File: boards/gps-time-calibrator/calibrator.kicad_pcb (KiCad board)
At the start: 4 copper layers, 180 x 100 mm, 374 parts, among them J1 DF40C-40DP-0.4V(51), J2 DF40C(2.0)-40DS-0.4V(51), J3 USB-C 5V/3A + DATA, J5 GPS ANTENNA, J6 INPUT 5V / 2.5V THRESHOLD, J7 FPGA OUTPUT 5V, J8 61300411121, Q1 AO3400A, Q10 AO3400A, Q11 AO3400A, Q12 AO3400A, Q13 AO3400A, Q14 AO3400A, Q15 AO3400A, Q16 AO3400A, Q2 AO3400A, Q3 AO3400A, Q4 AO3400A, Q5 AO3400A, Q6 AO3400A, Q7 AO3400A, Q8 AO3400A, Q9 AO3400A, U1 USBLC6-2SC6, U10 SN74AHCT1G125DBVR, U11 HUSB238_002DD, U12 AP2112K-3.3, U14 TPS259531DSGR, U15 TPS7A4533DCQR, U2 AP2112K-3.3, U3 SN74LVC541APWR, U4 SN74LVC541APWR, U5 AP2112K-3.3, U6 MAX-M10S-00B-01, U7 SN74LVC1G17DBVR, U9 TLV3501AIDBVR, Y1 AOC97FAJC-10.0000

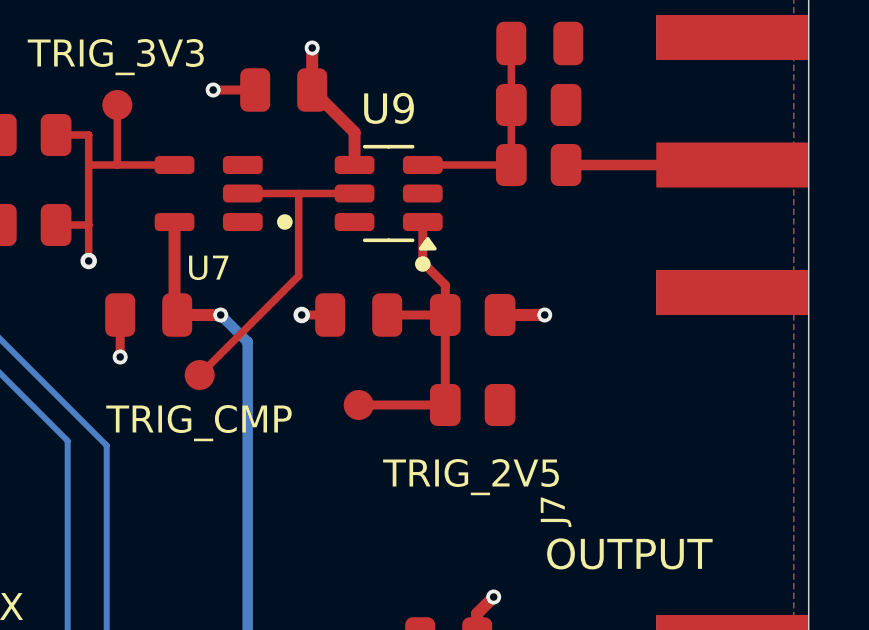
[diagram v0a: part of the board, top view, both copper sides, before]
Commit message: Stack the 2.5 V threshold network under the trigger input RC
R160, R161 and C13 now continue the C75/R9/R8 column: horizontal, same
x, 2.0 mm pitch. Their TRIGGER_VREF pads share one vertical bus on the
left that takes U9 pin 1 straight across and runs down (45-degree corner)
to the TRIG_2V5 pad. The old VIN via beside R160 and the GND via beside
C13 are removed; R160's 5 V pad gets a single via right next to it into
the In2 plane, and the GND pads use the pour.

ERC 0, DRC 0 with parity; lint 671 -> 669 (none added); quality
unchanged.

Co-Authored-By: Claude Opus 5.5 <noreply@anthropic.com>
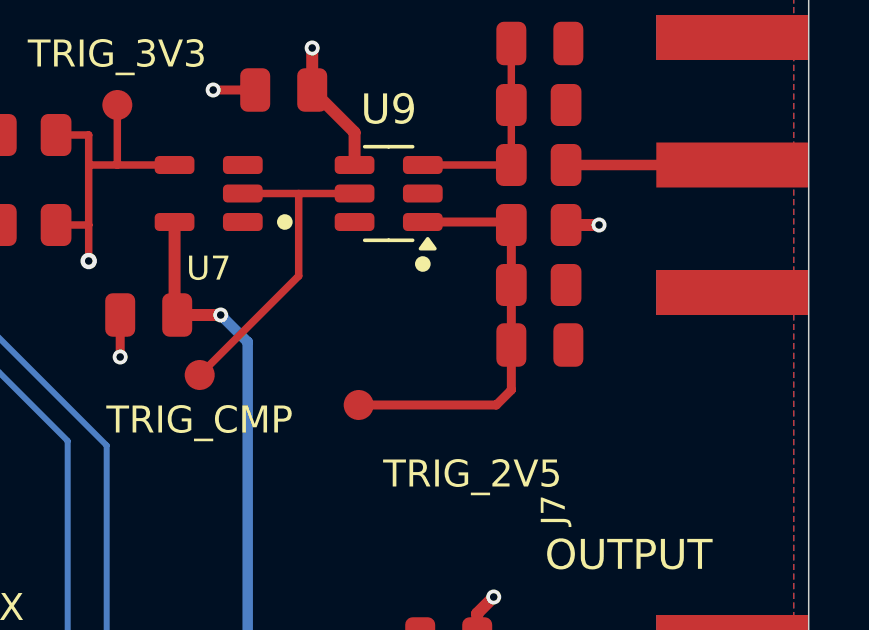
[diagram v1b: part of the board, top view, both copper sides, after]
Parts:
- moved C13 6.12 mm to (191.0, 56.0), turned to 0 degrees
- moved R161 4.57 mm to (191.0, 54.0)
- moved R160 3.72 mm to (191.0, 52.0)
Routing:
- net TRIGGER_VREF: track 11.2 -> 13.8 mm
- net GND: track 169.7 -> 168.7 mm, vias 138 -> 137
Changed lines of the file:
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@@
 	(footprint "Calibrator:R_0805_2012Metric"
 		(layer "F.Cu")
-		(at 188.8 58)
+		(at 191 54)
 		(descr "Lower 10 kOhm of the divider setting the 2.5 V trigger threshold.")
 		(tags "resistor")
@@
 	(footprint "Calibrator:R_0805_2012Metric"
 		(layer "F.Cu")
-		(at 188.8 55 180)
+		(at 191 52 180)
 		(descr "Upper 10 kOhm of the divider setting the 2.5 V trigger threshold from 5 V.")
 		(tags "resistor")
@@
 	(footprint "Calibrator:C_0805_2012Metric"
 		(layer "F.Cu")
-		(at 185 55 180)
+		(at 191.038 56)
 		(descr "100 nF filter on the 2.5 V trigger threshold.")
 		(tags "capacitor")
 		(property "Reference" "C13"
-			(at -2.8 0 270)
+			(at -2.8 0 90)
 			(layer "F.SilkS")
 			(hide yes)
@@
 		)
 		(property "Value" "100nF"
-			(at 0 1.68 180)
+			(at 0 1.68 0)
 			(layer "F.Fab")
 			(hide yes)
@@
 		)
 		(property "Datasheet" ""
-			(at 0 0 180)
+			(at 0 0 0)
 			(layer "F.Fab")
 			(hide yes)
@@
 		)
 		(property "Description" ""
-			(at 0 0 180)
+			(at 0 0 0)
 			(layer "F.Fab")
 			(hide yes)
@@
 		)
 		(property "MPN" "CL21B104KBCNNNC"
-			(at 0 0 180)
+			(at 0 0 0)
 			(layer "F.SilkS")
 			(hide yes)
@@
 		)
 		(property "LCSC" "C1711"
-			(at 0 0 180)
+			(at 0 0 0)
 			(layer "F.SilkS")
 			(hide yes)
@@
 		)
 		(property "Assembly" "JLCPCB"
-			(at 0 0 180)
+			(at 0 0 0)
 			(layer "F.SilkS")
 			(hide yes)
@@
 		)
 		(property "Supplier URL" ""
-			(at 0 0 180)
+			(at 0 0 0)
 			(layer "F.SilkS")
 			(hide yes)
@@
 		(duplicate_pad_numbers_are_jumpers no)
 		(fp_line
-			(start 1.7 0.98)
-			(end -1.7 0.98)
+			(start -1.7 -0.98)
+			(end 1.7 -0.98)
 			(stroke
 				(width 0.05)
@@
 		)
 		(fp_line
-			(start 1.7 -0.98)
-			(end 1.7 0.98)
+			(start -1.7 0.98)
+			(end -1.7 -0.98)
 			(stroke
 				(width 0.05)
@@
 		)
 		(fp_line
-			(start -1.7 0.98)
-			(end -1.7 -0.98)
+			(start 1.7 -0.98)
+			(end 1.7 0.98)
 			(stroke
 				(width 0.05)
@@
 		)
 		(fp_line
-			(start -1.7 -0.98)
-			(end 1.7 -0.98)
+			(start 1.7 0.98)
+			(end -1.7 0.98)
 			(stroke
 				(width 0.05)
@@
 		)
 		(fp_line
-			(start 1 0.625)
-			(end -1 0.625)
+			(start -1 -0.625)
+			(end 1 -0.625)
 			(stroke
 				(width 0.1)
@@
 		)
 		(fp_line
-			(start 1 -0.625)
-			(end 1 0.625)
+			(start -1 0.625)
+			(end -1 -0.625)
 			(stroke
 				(width 0.1)
@@
 		)
 		(fp_line
-			(start -1 0.625)
-			(end -1 -0.625)
+			(start 1 -0.625)
+			(end 1 0.625)
 			(stroke
 				(width 0.1)
@@
 		)
 		(fp_line
-			(start -1 -0.625)
-			(end 1 -0.625)
+			(start 1 0.625)
+			(end -1 0.625)
 			(stroke
 				(width 0.1)
@@
 		)
 		(fp_text user "${REFERENCE}"
-			(at 0 0 180)
+			(at 0 0 0)
 			(layer "F.Fab")
 			(effects
@@
 		)
 		(pad "1" smd roundrect
-			(at -0.95 0 180)
+			(at -0.95 0)
 			(size 1 1.45)
 			(layers "F.Cu" "F.Mask" "F.Paste")
@@
 		)
 		(pad "2" smd roundrect
-			(at 0.95 0 180)
+			(at 0.95 0)
 			(size 1 1.45)
 			(layers "F.Cu" "F.Mask" "F.Paste")
@@
 	)
 	(segment
-		(start 189.7125 55)
-		(end 191.2 55)
-		(width 0.4)
-		(layer "F.Cu")
-		(net "VIN_5V")
-	)
-	(segment
 		(start 68 88.825)
 		(end 68 90.025)
@@
 	)
 	(segment
+		(start 191.912 52)
+		(end 193.012 52)
+		(width 0.4)
+		(layer "F.Cu")
+		(net "VIN_5V")
+	)
+	(segment
 		(start 50 64.825)
 		(end 50 66.025)
@@
 	)
 	(via
+		(at 193.012 52)
+		(size 0.5)
+		(drill 0.25)
+		(layers "F.Cu" "B.Cu")
+		(net "VIN_5V")
+	)
+	(via
 		(at 64.5 54.4)
 		(size 0.5)
@@
 		(net "VIN_5V")
 	)
-	(via
-		(at 191.2 55)
-		(size 0.5)
-		(drill 0.25)
-		(layers "F.Cu" "B.Cu")
-		(net "VIN_5V")
-	)
 	(segment
 		(start 104 85.4)
@@
 	)
 	(segment
-		(start 184.05 55)
-		(end 183.1 55)
-		(width 0.3)
-		(layer "F.Cu")
-		(net "GND")
-	)
-	(segment
 		(start 124.5 75.05)
 		(end 124.5 73.6)
@@
 	)
 	(via
-		(at 183.1 55)
-		(size 0.55)
-		(drill 0.25)
-		(layers "F.Cu" "B.Cu")
-		(net "GND")
-	)
-	(via
 		(at 46.5 49.6)
 		(size 0.5)
@@
 	)
 	(segment
-		(start 187.8875 55)
-		(end 187.8875 58)
-		(width 0.3)
-		(layer "F.Cu")
-		(net "TRIGGER_VREF")
-	)
-	(segment
-		(start 185.95 55)
-		(end 187.8875 55)
-		(width 0.3)
-		(layer "F.Cu")
-		(net "TRIGGER_VREF")
-	)
-	(segment
-		(start 187.1375 51.9)
-		(end 187.1375 53.25)
+		(start 189.588 58)
+		(end 185 58)
 		(width 0.3)
 		(layer "F.Cu")
@@
 	)
 	(segment
-		(start 185 58)
-		(end 187.8875 58)
+		(start 190.088 51.9)
+		(end 190.088 57.5)
 		(width 0.3)
 		(layer "F.Cu")
@@
 	)
 	(segment
-		(start 187.1375 53.25)
-		(end 187.8875 54)
+		(start 190.088 57.5)
+		(end 189.588 58)
 		(width 0.3)
 		(layer "F.Cu")
@@
 	)
 	(segment
-		(start 187.8875 54)
-		(end 187.8875 55)
+		(start 187.137 51.9)
+		(end 190.088 51.9)
 		(width 0.3)
 		(layer "F.Cu")

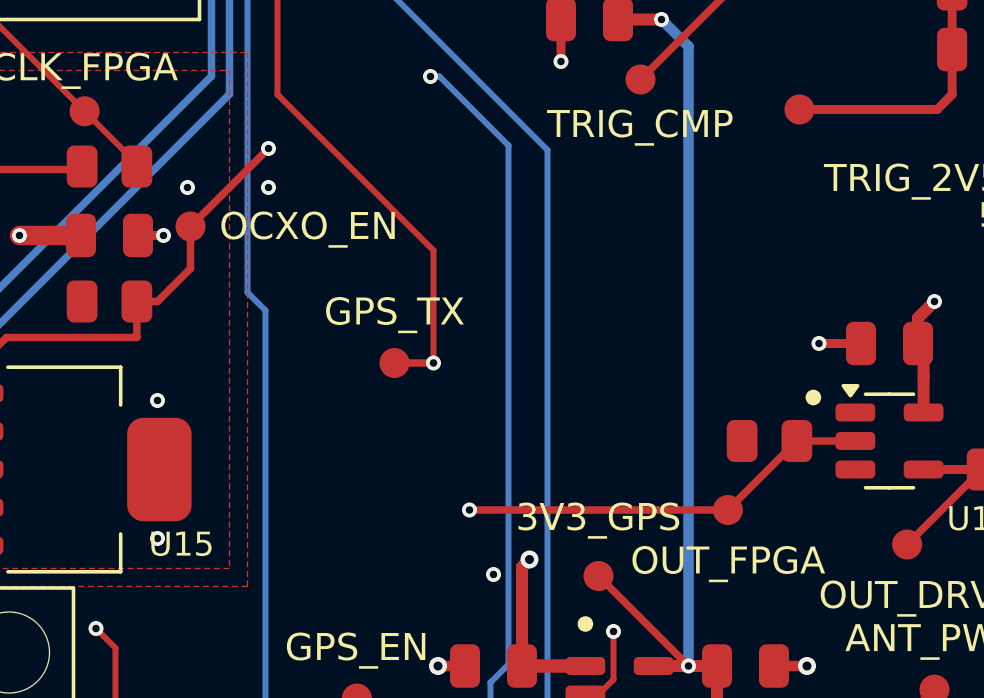
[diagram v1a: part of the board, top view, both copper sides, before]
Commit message: Straighten the FPGA_IOT_51A trigger route from J2 to U10
Drop J2.30 straight onto In2 so it clears the ESP_GPIO6/GPIO5 In1 verticals
without an In1-In2-In1 hop, change to In1 once, and run straight to a via
above R163. R163.1 now exits vertically and TP23 hangs off a 45-degree miter
below it instead of the route dipping to y 71.35 and climbing back. Four vias
become three; DRC/ERC clean, lint 669 -> 668.

Co-Authored-By: Claude Opus 5.5 <noreply@anthropic.com>
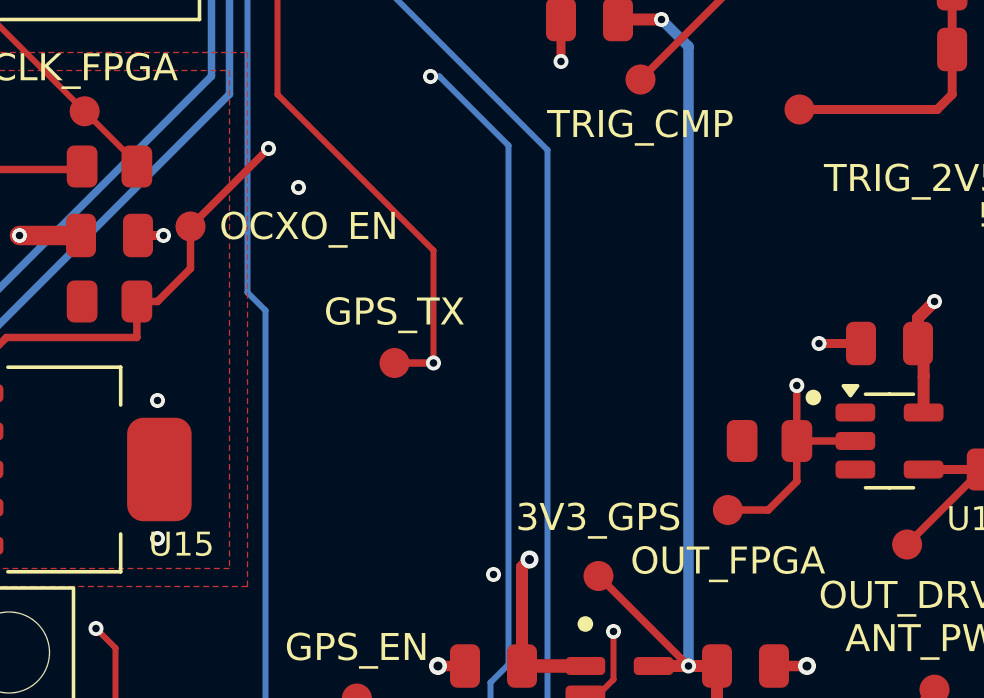
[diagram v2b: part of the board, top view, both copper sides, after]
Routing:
- net FPGA_IOT_51A: track 47.7 -> 48.0 mm, vias 4 -> 3
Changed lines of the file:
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@@
 	)
 	(segment
-		(start 182.6125 71.35)
-		(end 184.9125 69.05)
+		(start 184.91 67.2)
+		(end 184.91 70.4)
 		(width 0.25)
 		(layer "F.Cu")
@@
 	)
 	(segment
-		(start 174 71.35)
-		(end 182.6125 71.35)
+		(start 184.91 70.4)
+		(end 183.96 71.35)
+		(width 0.25)
+		(layer "F.Cu")
+		(net "FPGA_IOT_51A")
+	)
+	(segment
+		(start 183.96 71.35)
+		(end 182.61 71.35)
 		(width 0.25)
 		(layer "F.Cu")
@@
 	)
 	(via
-		(at 164.6 60.6)
+		(at 184.91 67.2)
 		(size 0.5)
 		(drill 0.25)
@@
 	)
 	(via
-		(at 174 71.35)
-		(size 0.5)
-		(drill 0.25)
-		(layers "F.Cu" "B.Cu")
-		(net "FPGA_IOT_51A")
-	)
-	(via
-		(at 167.3 60.6)
+		(at 168.3 60.6)
 		(size 0.5)
 		(drill 0.25)
@@
 	)
 	(segment
-		(start 154.8 56)
-		(end 160 56)
-		(width 0.25)
-		(layer "In1.Cu")
-		(net "FPGA_IOT_51A")
-	)
-	(segment
-		(start 167.3 60.6)
-		(end 168.3 60.6)
-		(width 0.25)
-		(layer "In1.Cu")
-		(net "FPGA_IOT_51A")
-	)
-	(segment
-		(start 174 66.3)
-		(end 174 71.35)
-		(width 0.25)
-		(layer "In1.Cu")
-		(net "FPGA_IOT_51A")
-	)
-	(segment
-		(start 160 56)
-		(end 164.6 60.6)
+		(start 174.9 67.2)
+		(end 184.91 67.2)
 		(width 0.25)
 		(layer "In1.Cu")
@@
 	(segment
 		(start 168.3 60.6)
-		(end 174 66.3)
+		(end 174.9 67.2)
 		(width 0.25)
 		(layer "In1.Cu")
@@
 	)
 	(segment
-		(start 164.6 60.6)
-		(end 167.3 60.6)
+		(start 159.4 60.6)
+		(end 168.3 60.6)
 		(width 0.25)
 		(layer "In2.Cu")
+		(net "FPGA_IOT_51A")
+	)
+	(segment
+		(start 154.8 56)
+		(end 159.4 60.6)
+		(width 0.25)
+		(layer "In2.Cu")

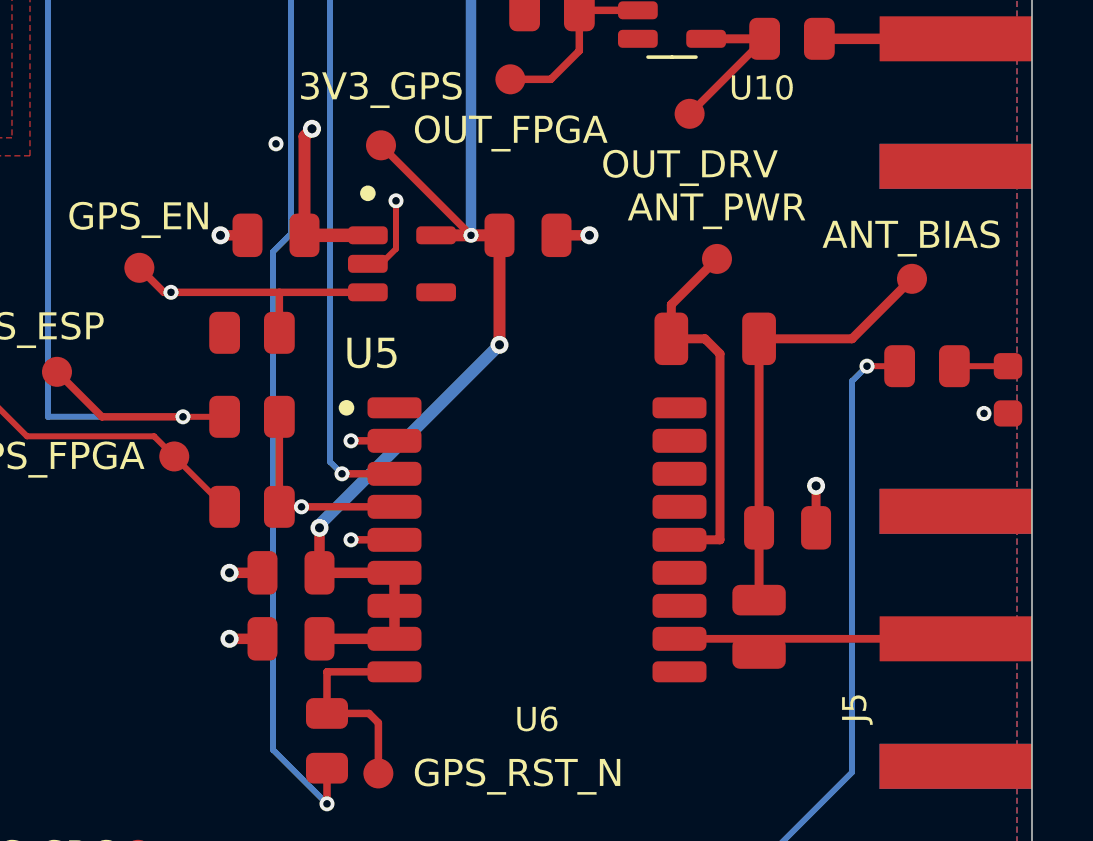
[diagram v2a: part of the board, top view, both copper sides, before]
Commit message: Line up the GPS passives beside U6, stand R5 above C10, drop TP28/TP29
R177, R7, R6, C9 and C8 now share one column at x 175.2 mm. The resistors
moved right onto the decoupling caps' line so C9/C8 stay tight to U6. The
GPS_PPS In1 via that would have sat in R6.1 moves to the gap between R7 and
R6, and the +3V3_GPS B.Cu feed via moves onto the C9 -> U6.6 trace.

R5 (antenna bias, 1206) is vertical in the C10/L1 column: ANT_BIAS drops
straight from R5.2 through C10 to L1, and ANT_PWR leaves U6.14 square and
climbs at x 189.6 into R5.1. TP28 (ANT_PWR) and TP29 (ANT_BIAS) are removed
from the board, circuit.json, the regenerated schematic/PDF, the testpoint
map/CSV/JSON/audit, final placements and part descriptions; 28 pads remain.

ERC 0, DRC 0 with 0 parity issues; lint 668 -> 665 (none added); quality
warnings 14335 -> 14331, errors unchanged at 64.

Co-Authored-By: Claude Opus 5.5 <noreply@anthropic.com>
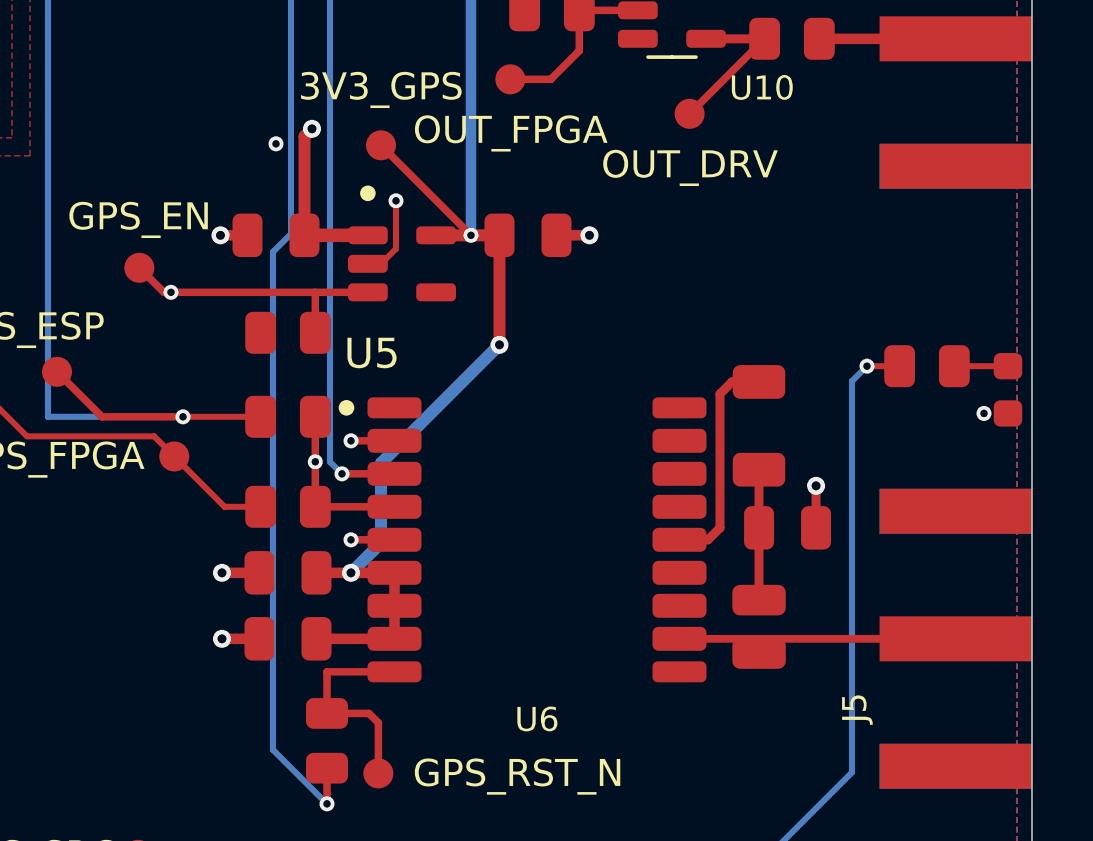
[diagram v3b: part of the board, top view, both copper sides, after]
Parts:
- removed TP28: ANT_PWR, Calibrator:TP_1p0mm
- removed TP29: ANT_BIAS, Calibrator:TP_1p0mm
- moved R5 3.25 mm to (190.9, 82.9), turned to -90 degrees
- moved R177 1.20 mm to (175.2, 79.8)
- moved R6 1.20 mm to (175.2, 85.6)
- moved R7 1.20 mm to (175.2, 82.6)
- moved C8 0.10 mm to (175.2, 90.0)
- moved C9 0.10 mm to (175.2, 87.8)
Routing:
- net ANT_BIAS: track 14.6 -> 4.35 mm
- net ANT_PWR: track 12.7 -> 7.44 mm
- net ESP_GPIO38: track 74.1 -> 75.3 mm
- net FPGA_IOT_46B_G0: track 49.2 -> 50.4 mm
